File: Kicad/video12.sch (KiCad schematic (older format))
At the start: 18 parts, among them J20 DE15HD, U19 THS7316, U20 TPD7S019

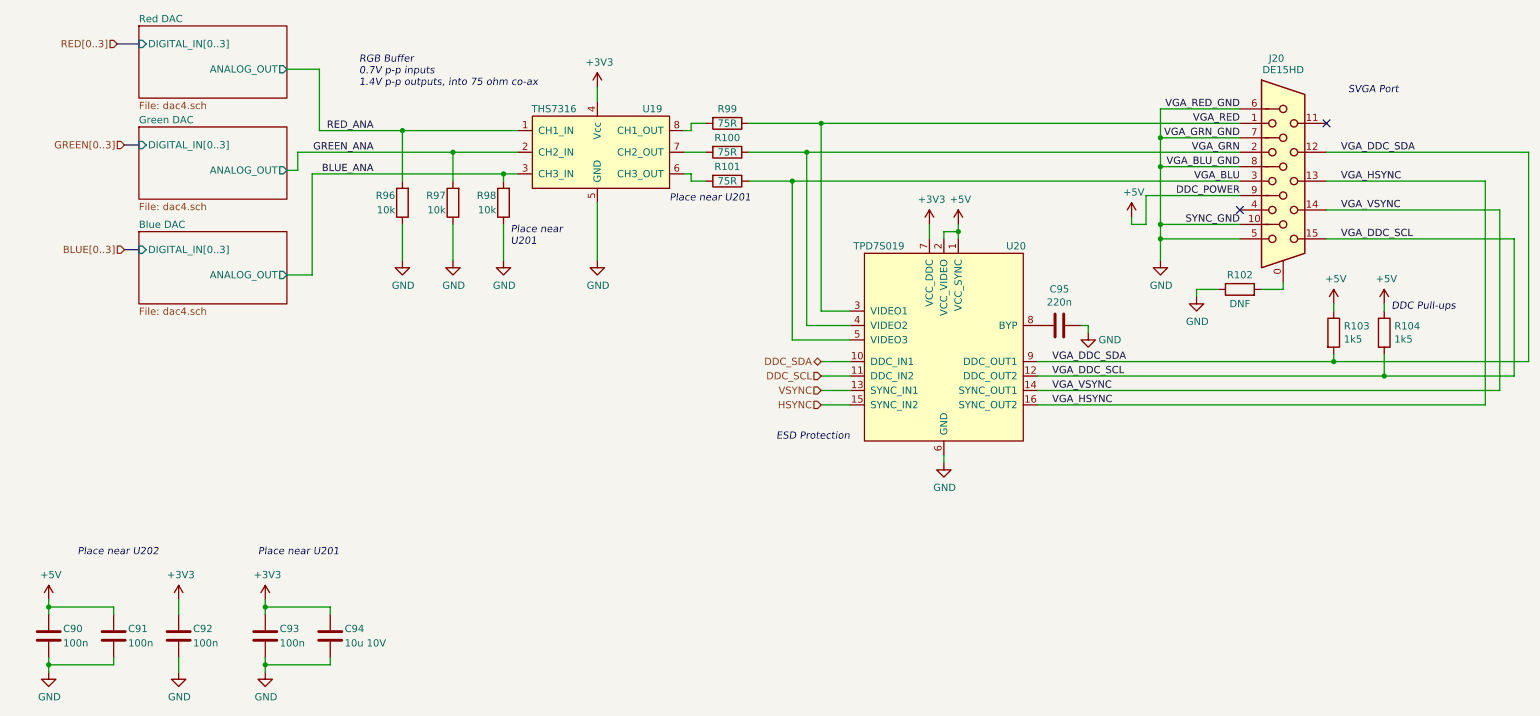
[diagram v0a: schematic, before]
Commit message: Add 4-bit Video DAC, and re-wire BMC.
Now the BMC is an SPI device, and has a four-wire UART.
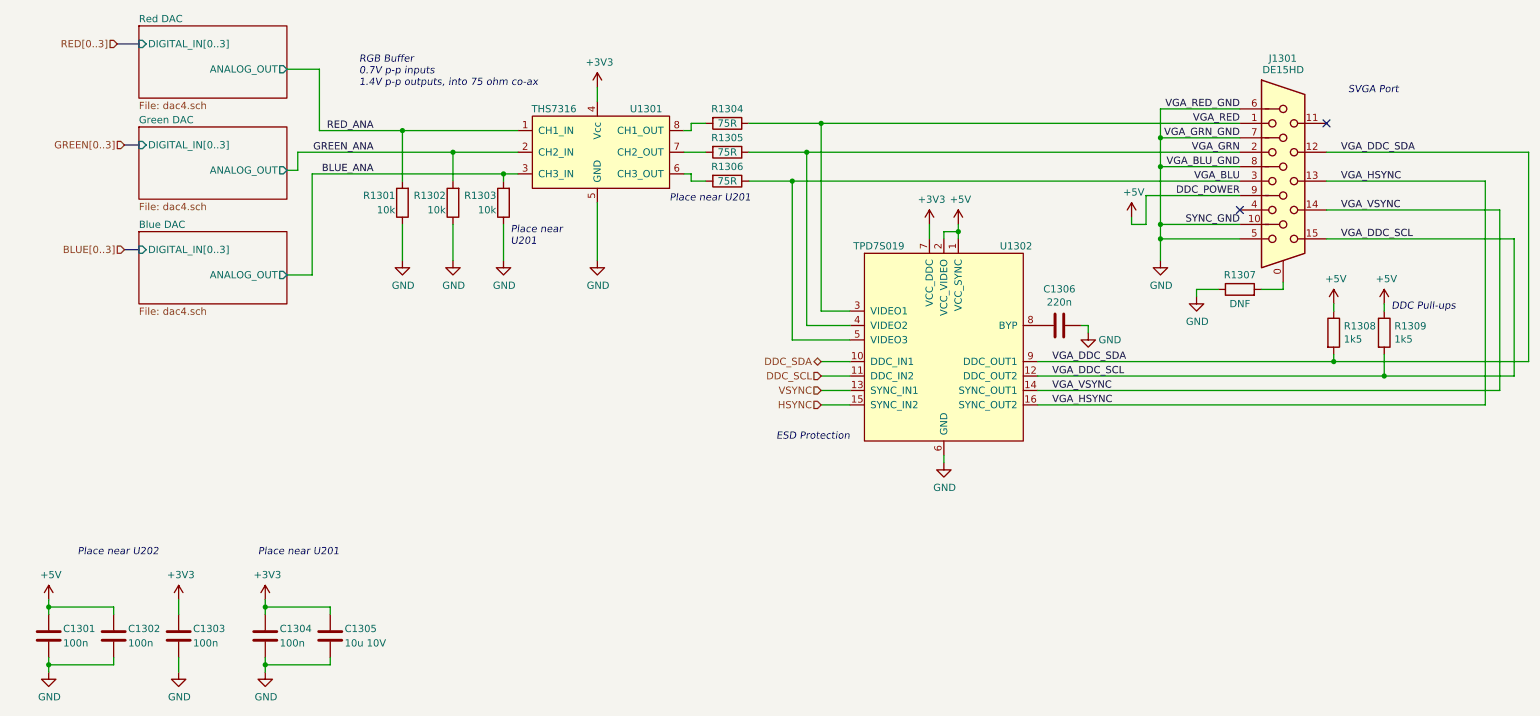
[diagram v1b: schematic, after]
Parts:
- renumbered C90 to C1301, C91 to C1302, C92 to C1303, C93 to C1304, C94 to C1305, C95 to C1306, J20 to J1301, R96 to R1301, R97 to R1302, R98 to R1303, R99 to R1304, R100 to R1305, R101 to R1306, R102 to R1307, R103 to R1308, R104 to R1309, U19 to U1301, U20 to U1302

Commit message: Tidy up part nos and swapped I2C/UART on BMC.
Mark all resistors as 1% if not specified.
Added some Mouser part numbers.
BMC can now be programmed over UART.
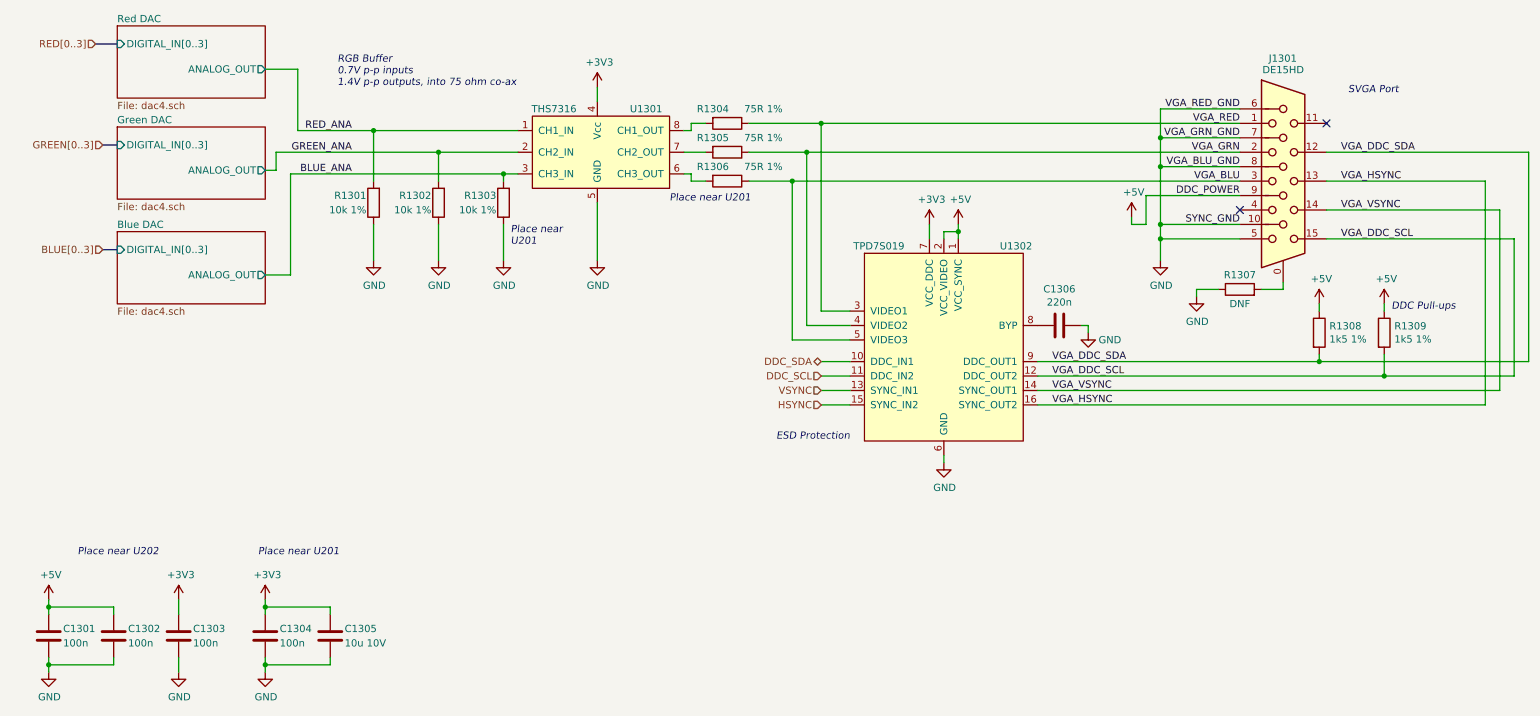
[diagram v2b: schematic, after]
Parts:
- C1301, C1302, C1303, C1304: Mouser (none) -> 594-K104K15X7RF5TL2
- J1301: Mouser (none) -> 649-ICD15S13E4GV00LF
- R1301, R1302, R1303: value 10k -> 10k 1%
- R1304, R1305, R1306: value 75R -> 75R 1%
- R1308, R1309: value 1k5 -> 1k5 1%
- U1301: Mouser (none) -> 595-THS7316DR
- U1302: Mouser (none) -> 595-TPD7S019-15DBQR
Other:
- moved on the sheet: R1301, R1302, R1308

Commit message: Changes to BMC
* Swapped BUTTON_PWR and SYS_RESET to avoid DRC issue
* Split PSU and BMC into two separate sheets
* Swapped some pins on the STM32 to make it compatible with more
alternatives
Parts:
- renumbered C1301 to C1201, C1302 to C1202, C1303 to C1203, C1304 to C1204, C1305 to C1205, C1306 to C1206, J1301 to J1201, R1301 to R1201, R1302 to R1202, R1303 to R1203, R1304 to R1204, R1305 to R1205, R1306 to R1206, R1307 to R1207, R1308 to R1208, R1309 to R1209, U1301 to U1201, U1302 to U1202
